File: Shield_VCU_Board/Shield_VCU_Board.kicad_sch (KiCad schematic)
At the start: 184 parts, among them J1 Conn_02x10_Odd_Even, J10 Main_Supply, J11 Molex_connector_40pin, J12 TFT Wire, J13 Molex_x06_Socket, J15 Conn_01x04_Socket, J2 Conn_02x10_Odd_Even, J3 Conn_02x09_Odd_Even, J4 Conn_02x09_Odd_Even, J5 Conn_02x09_Odd_Even, J6 Conn_02x10_Odd_Even, J7 Button_Activation_Logic, J8 Conn_ToSpeaker, J9 Wire_x06_Pin, U1 AS1115-BSST, U2 SN74LVC1G125DBV, U3 MC74HC14A, U4 TPA6205A1, U5 TLV76133DCY, U6 TLV76150DCY, U7 FT812, U8 TLV76133DCY, U9 TLV76133DCY, Y1 12MHz, Y2 SGM3766YTN5G

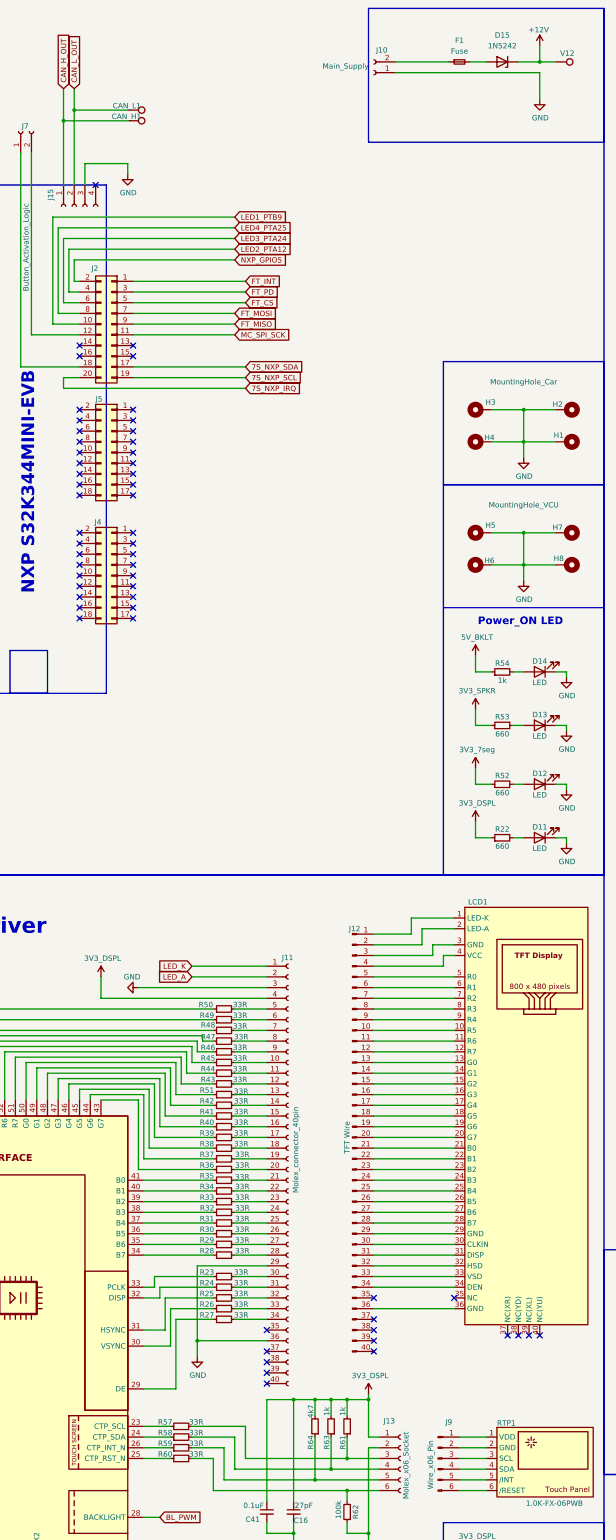
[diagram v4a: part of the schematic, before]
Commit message: Updated Display Driver pins
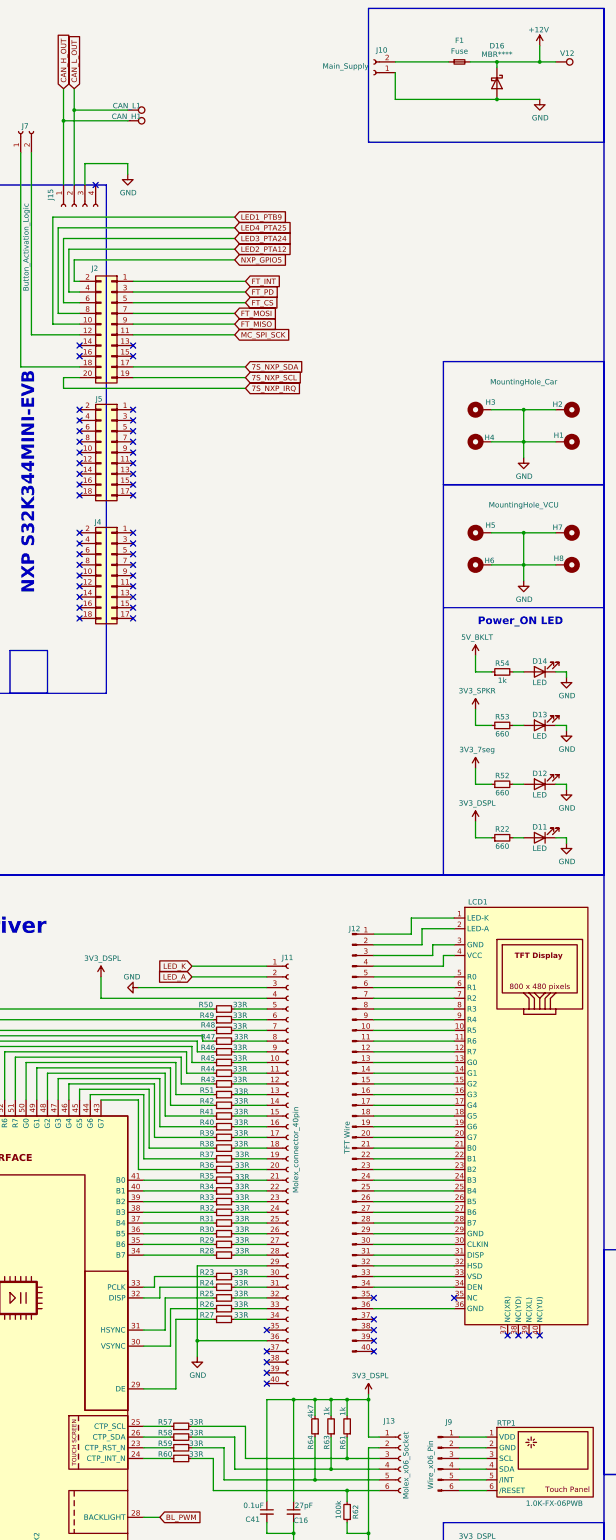
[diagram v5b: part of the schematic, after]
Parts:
- removed D15: 1N5242, Diode_THT:D_DO-201_P15.24mm_Horizontal, symbol Diode:1N53xxB
- added D16: MBR****, Diode_SMD:D_SOD-123, symbol Diode:MBR0540
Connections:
- net +12V: now also F1.2, D16.1 (K)
- net GND: now also D16.2 (A)
- net at R60.1: now also U7.24 (CTP_INT_N); no longer U7.25 (CTP_RST_N)
- net at R57.1: now also U7.25 (CTP_SCL); no longer U7.23 (CTP_SCL)
- net at R58.1: now also U7.26 (CTP_SDA); no longer U7.24 (CTP_SDA)
- net at R59.1: now also U7.23 (CTP_RST_N); no longer U7.26 (CTP_INT_N)
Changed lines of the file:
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@@
 	)
 	(junction
+		(at 190.5 34.29)
+		(diameter 0)
+		(color 0 0 0 0)
+	)
+	(junction
 		(at 388.62 397.51)
 		(diameter 0)
@@
 	)
 	(junction
+		(at 200.66 25.4)
+		(diameter 0)
+		(color 0 0 0 0)
+	)
+	(junction
 		(at 307.34 222.25)
 		(diameter 0)
@@
 	)
 	(junction
-		(at 200.66 25.4)
-		(diameter 0)
-		(color 0 0 0 0)
-	)
-	(junction
 		(at 312.42 381)
 		(diameter 0)
@@
 	)
 	(junction
+		(at 190.5 25.4)
+		(diameter 0)
+		(color 0 0 0 0)
+	)
+	(junction
 		(at 252.73 392.43)
 		(diameter 0)
@@
 	(wire
 		(pts
+			(xy 190.5 25.4) (xy 200.66 25.4)
+		)
+		(stroke
+			(width 0)
+			(type default)
+		)
+	)
+	(wire
+		(pts
 			(xy 106.68 295.91) (xy 123.19 295.91)
 		)
@@
 	(wire
 		(pts
+			(xy 190.5 26.67) (xy 190.5 25.4)
+		)
+		(stroke
+			(width 0)
+			(type default)
+		)
+	)
+	(wire
+		(pts
 			(xy 274.32 381) (xy 273.05 381)
 		)
@@
 	(wire
 		(pts
-			(xy 200.66 27.94) (xy 200.66 34.29)
-		)
-		(stroke
-			(width 0)
-			(type default)
-		)
-	)
-	(wire
-		(pts
 			(xy 118.11 354.33) (xy 125.73 354.33)
 		)
@@
 		)
 	)
+	(wire
+		(pts
+			(xy 184.15 25.4) (xy 190.5 25.4)
+		)
+		(stroke
+			(width 0)
+			(type default)
+		)
+	)
 	(polyline
 		(pts
@@
 	(wire
 		(pts
-			(xy 195.58 25.4) (xy 200.66 25.4)
-		)
-		(stroke
-			(width 0)
-			(type default)
-		)
-	)
-	(wire
-		(pts
 			(xy 118.11 262.89) (xy 123.19 262.89)
 		)
@@
 	(wire
 		(pts
-			(xy 184.15 25.4) (xy 187.96 25.4)
-		)
-		(stroke
-			(width 0)
-			(type default)
-		)
-	)
-	(wire
-		(pts
 			(xy 533.4 269.24) (xy 541.02 269.24)
 		)
@@
 	(wire
 		(pts
-			(xy 166.37 27.94) (xy 200.66 27.94)
+			(xy 166.37 34.29) (xy 190.5 34.29)
 		)
 		(stroke
@@
 		)
 	)
+	(wire
+		(pts
+			(xy 166.37 34.29) (xy 166.37 27.94)
+		)
+		(stroke
+			(width 0)
+			(type default)
+		)
+	)
 	(polyline
 		(pts
@@
 	(wire
 		(pts
+			(xy 190.5 34.29) (xy 200.66 34.29)
+		)
+		(stroke
+			(width 0)
+			(type default)
+		)
+	)
+	(wire
+		(pts
 			(xy 123.19 356.87) (xy 118.11 356.87)
 		)
@@
 	)
 	(symbol
-		(lib_id "Diode:1N53xxB")
-		(at 191.77 25.4 180)
-		(unit 1)
-		(exclude_from_sim no)
-		(in_bom yes)
-		(on_board yes)
-		(dnp no)
-		(fields_autoplaced yes)
-		(property "Reference" "D15"
-			(at 191.77 19.05 0)
-			(effects
-				(font
-					(size 1.27 1.27)
-				)
-			)
-		)
-		(property "Value" "1N5242"
-			(at 191.77 21.59 0)
-			(effects
-				(font
-					(size 1.27 1.27)
-				)
-			)
-		)
-		(property "Footprint" "Diode_THT:D_DO-201_P15.24mm_Horizontal"
-			(at 191.77 20.955 0)
-			(effects
-				(font
-					(size 1.27 1.27)
-				)
-				(hide yes)
-			)
-		)
-		(property "Datasheet" "https://diotec.com/tl_files/diotec/files/pdf/datasheets/1n5345b.pdf"
-			(at 191.77 25.4 0)
-			(effects
-				(font
-					(size 1.27 1.27)
-				)
-				(hide yes)
-			)
-		)
-		(property "Description" "5000mW Zener Diode, DO-201"
-			(at 191.77 25.4 0)
-			(effects
-				(font
-					(size 1.27 1.27)
-				)
-				(hide yes)
-			)
-		)
-		(pin "2"
-		)
-		(pin "1"
-		)
-		(instances
-			(project ""
-				(path "/4a8cb20d-5f30-4163-a2c8-18e2deeb65d3"
-					(reference "D15")
-					(unit 1)
-				)
-			)
-		)
-	)
-	(symbol
 		(lib_id "Regulator_Linear:TLV76133DCY")
 		(at 551.18 332.74 0)
@@
 					(unit 1)
 				)
+			)
+		)
+	)
+	(symbol
+		(lib_id "Diode:MBR0540")
+		(at 190.5 30.48 270)
+		(unit 1)
+		(exclude_from_sim no)
+		(in_bom yes)
+		(on_board yes)
+		(dnp no)
+		(property "Reference" "D16"
+			(at 190.5 21.59 90)
+			(effects
+				(font
+					(size 1.27 1.27)
+				)
+			)
+		)
+		(property "Value" "MBR****"
+			(at 190.5 23.622 90)
+			(effects
+				(font
+					(size 1.27 1.27)
+				)
+			)
+		)
+		(property "Footprint" "Diode_SMD:D_SOD-123"
+			(at 186.055 30.48 0)
+			(effects
+				(font
+					(size 1.27 1.27)
+				)
+				(hide yes)
+			)
+		)
+		(property "Datasheet" "http://www.mccsemi.com/up_pdf/MBR0520~MBR0580(SOD123).pdf"
+			(at 190.5 30.48 0)
+			(effects
+				(font
+					(size 1.27 1.27)
+				)
+				(hide yes)
+			)
+		)
+		(property "Description" "40V 0.5A Schottky Power Rectifier Diode, SOD-123"
+			(at 190.5 30.48 0)
+			(effects
+				(font
+					(size 1.27 1.27)
+				)
+				(hide yes)
+			)
+		)
+		(pin "2"
+		)
+		(pin "1"
+		)
+		(instances
+			(project "Shield_VCU_Board"
+				(path "/4a8cb20d-5f30-4163-a2c8-18e2deeb65d3"
+					(reference "D16")
+					(unit 1)
+				)

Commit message: DWG cleanup
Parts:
- renumbered TP17 to AUDIOL1, TP13 to CS1, TP12 to INT1, TP15 to MISO1, TP14 to MOSI1, TP11 to PD1, R19 to RSET1, TP16 to SCK1
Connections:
- net NXP_GPIO5 renamed AUD_SHDN
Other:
- note added: "Main supply 12V"
- note removed: "AUDIO SHDN"
- moved on the sheet: AUDIOL1, AUDV3.3, BKLTV5, C1, C12, C13, C14, C15, C16, C17, C18, C19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

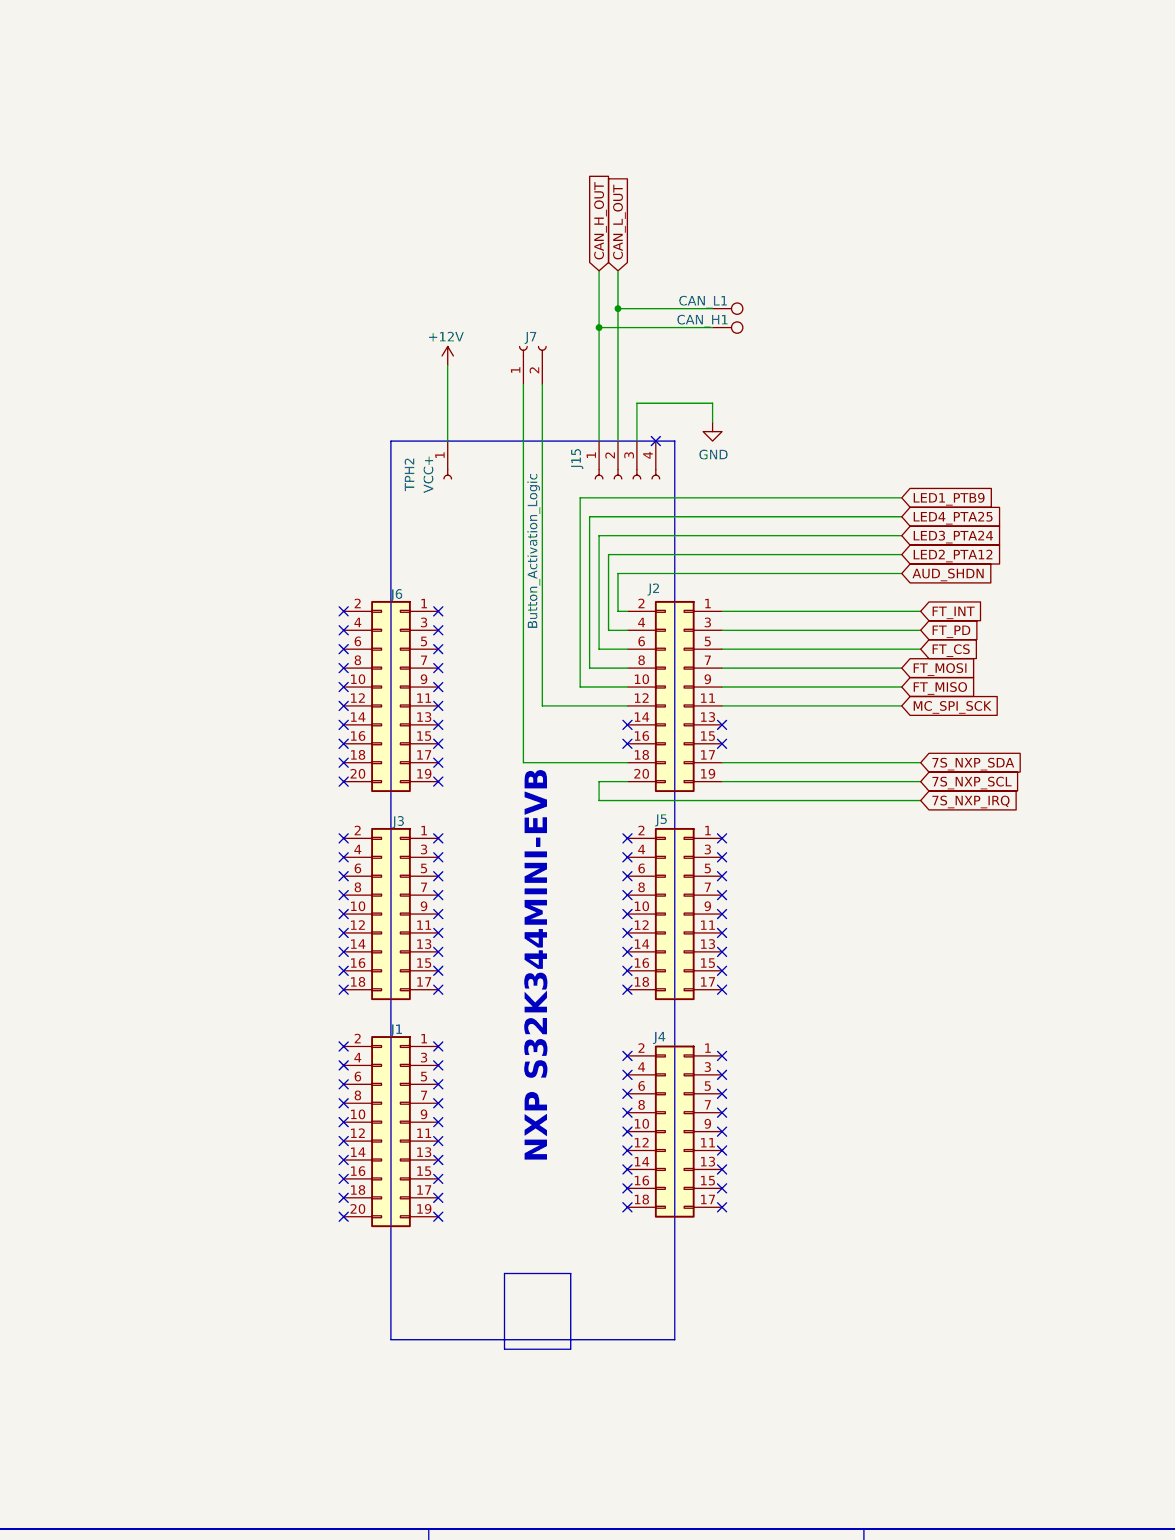
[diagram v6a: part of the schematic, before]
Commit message: BOM proto created
bill of materials added without the parts identified
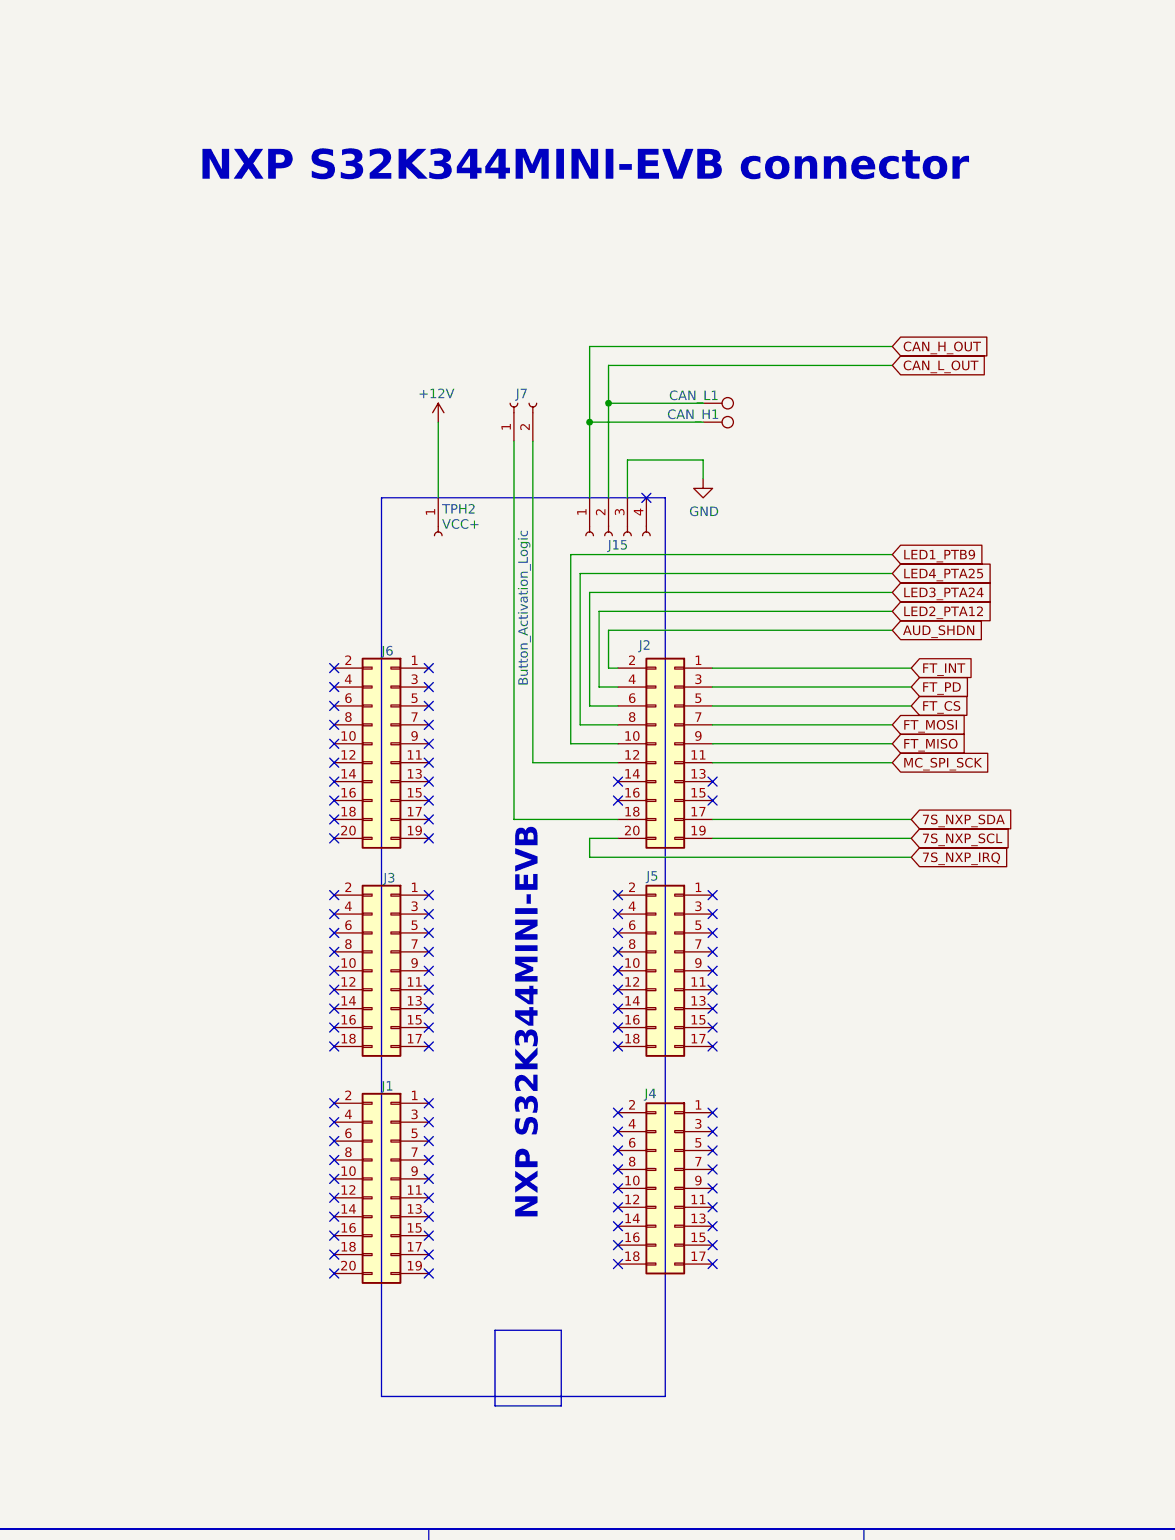
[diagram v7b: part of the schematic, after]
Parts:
- LCD1: value ~ -> LCD screen
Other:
- note added: "NXP S32K344MINI-EVB connector"
- moved on the sheet: CAN_H1, CAN_L1, J1, J15, J2, J3, J4, J5, J6, J7, TPH2

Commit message: RPP series added
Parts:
- removed D16: MBR****, Diode_SMD:D_SOD-123, symbol Diode:MBR0540
- added D15: MBRS340, Diode_SMD:D_SMC, symbol Diode:MBRS340
- F1: value Fuse -> Fuse_3A
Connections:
- net +12V: now also D15.1 (K); no longer F1.2
- new net: D15.2 (A), F1.2
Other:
- note added: "7 segment displ x8 + AS11*** driver"
- note added: "Capacitive Touch Panel"
- note removed: "7 segment displ 8x + driver"
- moved on the sheet: AUDV3.3, BKLTV5, C27, C28, C29, C30, C31, C32, C33, C34, D10, D7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
